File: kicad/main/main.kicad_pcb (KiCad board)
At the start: 2 copper layers, 98.5 x 119 mm, 11 parts, among them SW1 SW_SPDT_312, U1 HC-SR04, U2 DFR0654

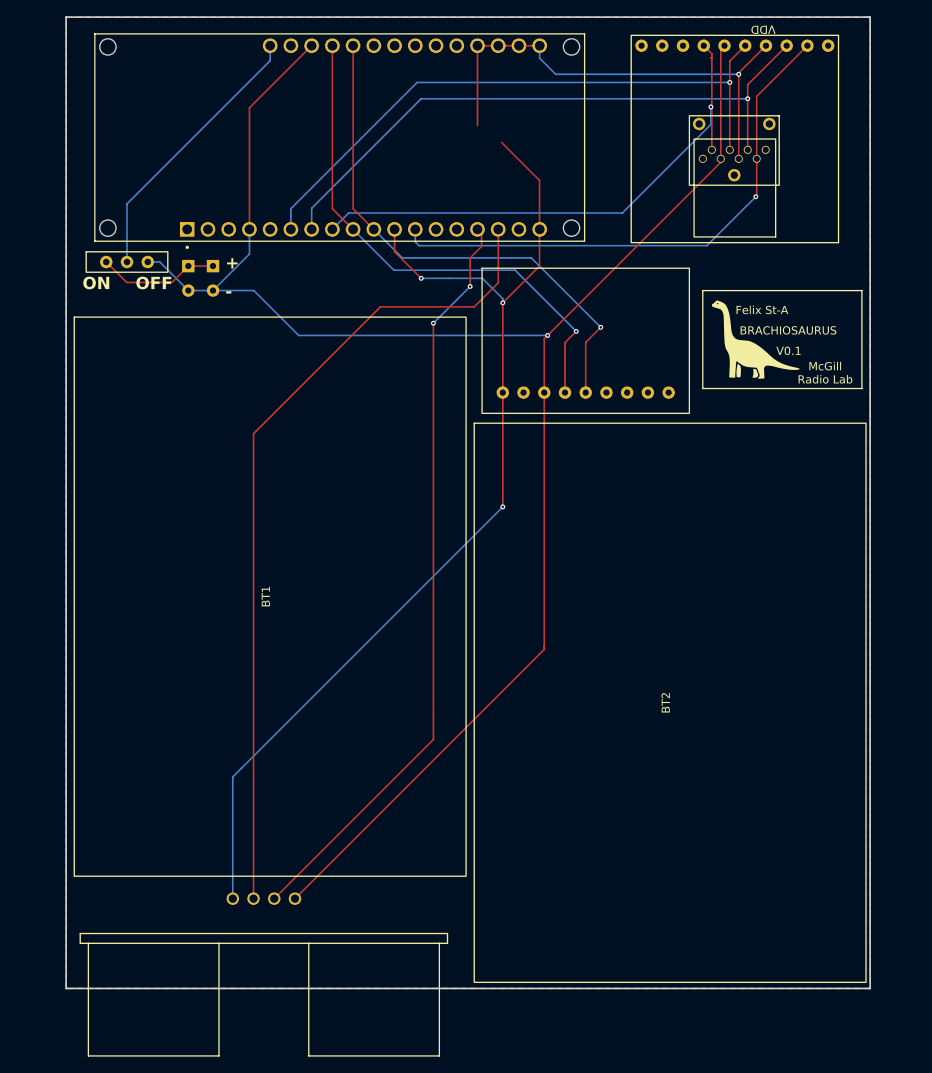
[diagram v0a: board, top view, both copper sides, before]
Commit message: cleaned up PCB design
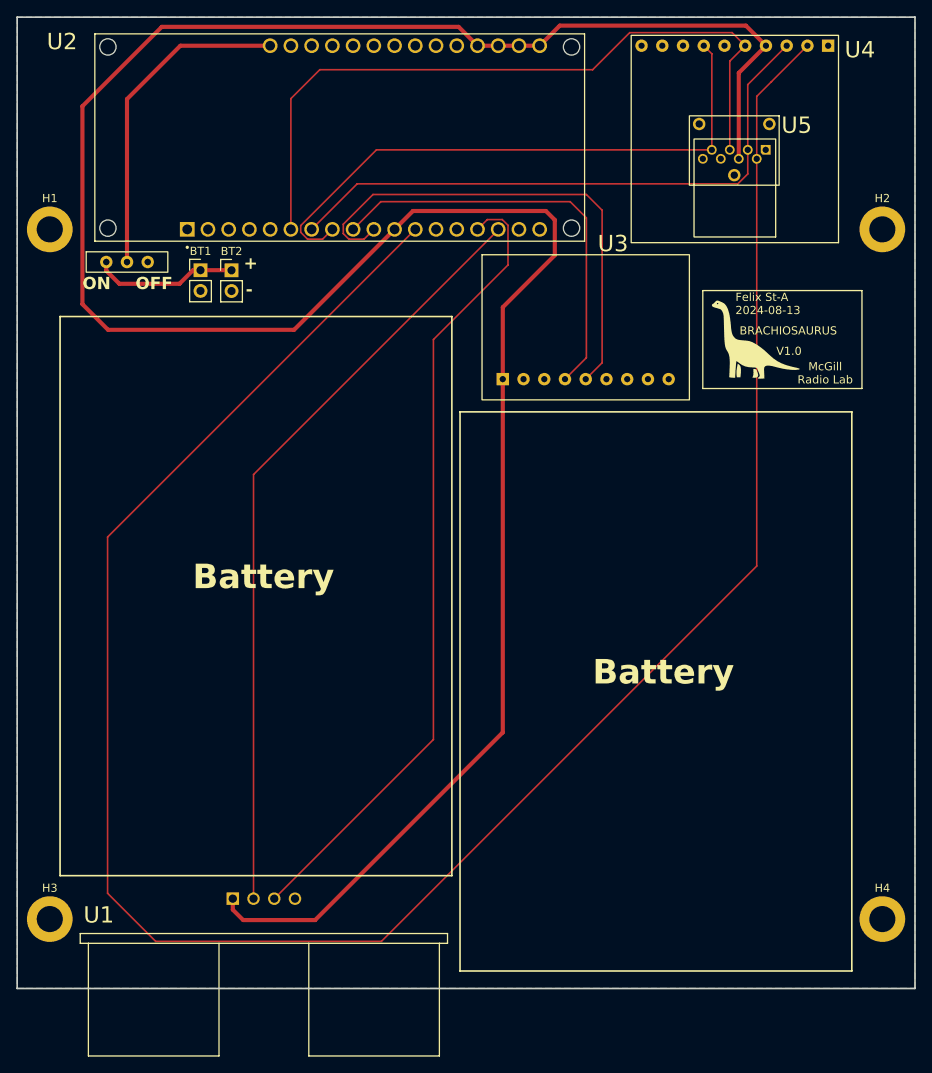
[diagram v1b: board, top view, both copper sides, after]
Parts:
- removed U6, U7: ~, singing foot:battery_holes
- added H1: MountingHole_Pad, MountingHole:MountingHole_3.2mm_M3_DIN965_Pad, F.Cu at (94.0, 65.0)
- added H2: MountingHole_Pad, MountingHole:MountingHole_3.2mm_M3_DIN965_Pad, F.Cu at (196.0, 65.0)
- added H3: MountingHole_Pad, MountingHole:MountingHole_3.2mm_M3_DIN965_Pad, F.Cu at (94.0, 149.5)
- added H4: MountingHole_Pad, MountingHole:MountingHole_3.2mm_M3_DIN965_Pad, F.Cu at (196.0, 149.5)
- BT1, BT2: value Battery_Cell -> Battery; footprint singing foot:batteries -> Connector_PinHeader_2.54mm:PinHeader_1x02_P2.54mm_Vertical
- moved BT2 75.5 mm to (116.3, 70.0), turned to 0 degrees
- moved BT1 40.9 mm to (112.5, 70.0), turned to 0 degrees
- moved U3 1.65 mm to (159.7, 77.0)
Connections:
- net Net-(U2-D7) renamed /SSD_CS
- net Net-(U2-MISO) renamed /MISO
- net Net-(U2-MOSI) renamed /MOSI
- net Net-(U2-SCK) renamed /SCLK
- SW1 pad 2: Net-(SW1-C) -> Net-(BT1-+)
- SW1 pad 3: Net-(SW1-A) -> unconnected-(SW1-A-Pad3)
- U1 pad 4: Net-(SW1-A) -> GND
- U2 pad 28: Net-(U3-SDA) -> unconnected-(U2-SDA-Pad28)
- U2 pad 29: Net-(U3-SCL) -> unconnected-(U2-SCL-Pad29)
- U2 pad 30: Net-(SW1-A) -> GND
- U2 pad 4: Net-(SW1-A) -> GND
- U3 pad 3: Net-(SW1-A) -> GND
- U4 pad 6: Net-(SW1-A) -> GND
- U5 pad 6: Net-(SW1-A) -> GND
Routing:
- net Net-(SW1-A): track 214.5 -> 0.00 mm, vias 1 -> 0
- net /SSD_CS: track 67.1 -> 264.3 mm, vias 1 -> 0
- net Net-(U1-VCC): track 188.4 -> 305.8 mm, vias 4 -> 0
- net Net-(BT1-+): track 0.00 -> 17.8 mm
- net Net-(SW1-C): track 15.0 -> 0.00 mm
- net /SCLK: track 76.3 -> 89.2 mm, vias 1 -> 0
- net Net-(U3-SCL): track 64.1 -> 51.6 mm, vias 1 -> 0
- net Net-(U1-TRIG): track 101.2 -> 94.4 mm
- net Net-(SW1-B): track 33.8 -> 40.2 mm
- net /MISO: track 67.1 -> 72.9 mm, vias 1 -> 0
- net Net-(U1-ECHO): track 93.0 -> 98.2 mm, vias 2 -> 0
- net Net-(U3-SDA): track 65.1 -> 61.2 mm, vias 1 -> 0
- net /MOSI: track 76.3 -> 73.9 mm, vias 1 -> 0
- net GND: track 0.00 -> 0.64 mm
- added copper zone on B.Cu, net GND
- removed copper zone on B.Cu, net (none)
- removed copper zone on F.Cu, net (none)
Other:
- board size 98.5 x 119 mm -> 110 x 119 mm
- board text added: "Battery"
- board text added: "Felix St-A 2024-08-13"
- board text added: "V1.0"
- board text removed: "Felix St-A"
- board text removed: "V0.1"

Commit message: as sent to PCBWay
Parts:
- BT1, BT2: footprint Connector_PinHeader_2.54mm:PinHeader_1x02_P2.54mm_Vertical -> Connector_Molex:Molex_KK-254_AE-6410-02A_1x02_P2.54mm_Vertical
- moved BT2 18.0 mm to (134.3, 70.0), turned to -90 degrees
- moved BT1 11.1 mm to (123.5, 70.0), turned to -90 degrees
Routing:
- net Net-(BT1-+): track 17.8 -> 38.0 mm
- net /SCLK: track 89.2 -> 79.9 mm
- net Net-(U1-VCC): track 305.8 -> 311.4 mm
